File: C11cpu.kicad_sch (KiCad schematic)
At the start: 29 parts, among them IC3 THVD1450DRBR, J1 V24 debug IF, J5 UDPI, U1 AVR64DA48, X1 ASE-24MHz

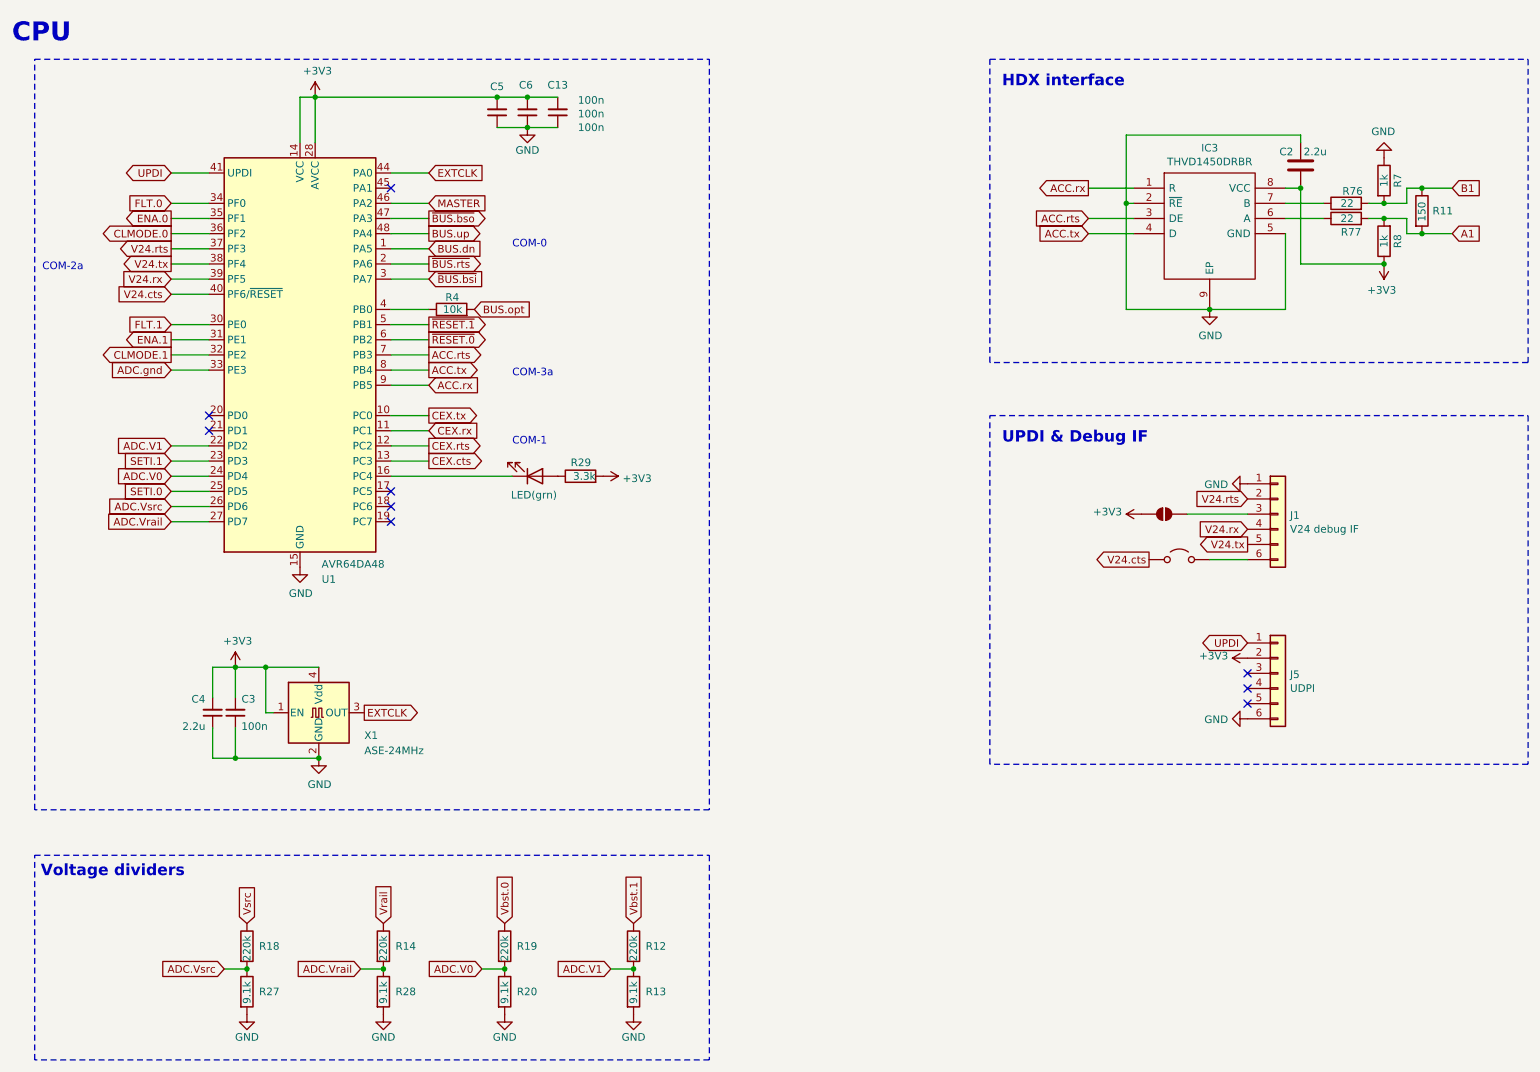
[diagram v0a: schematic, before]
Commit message: mod: changed to buck converter
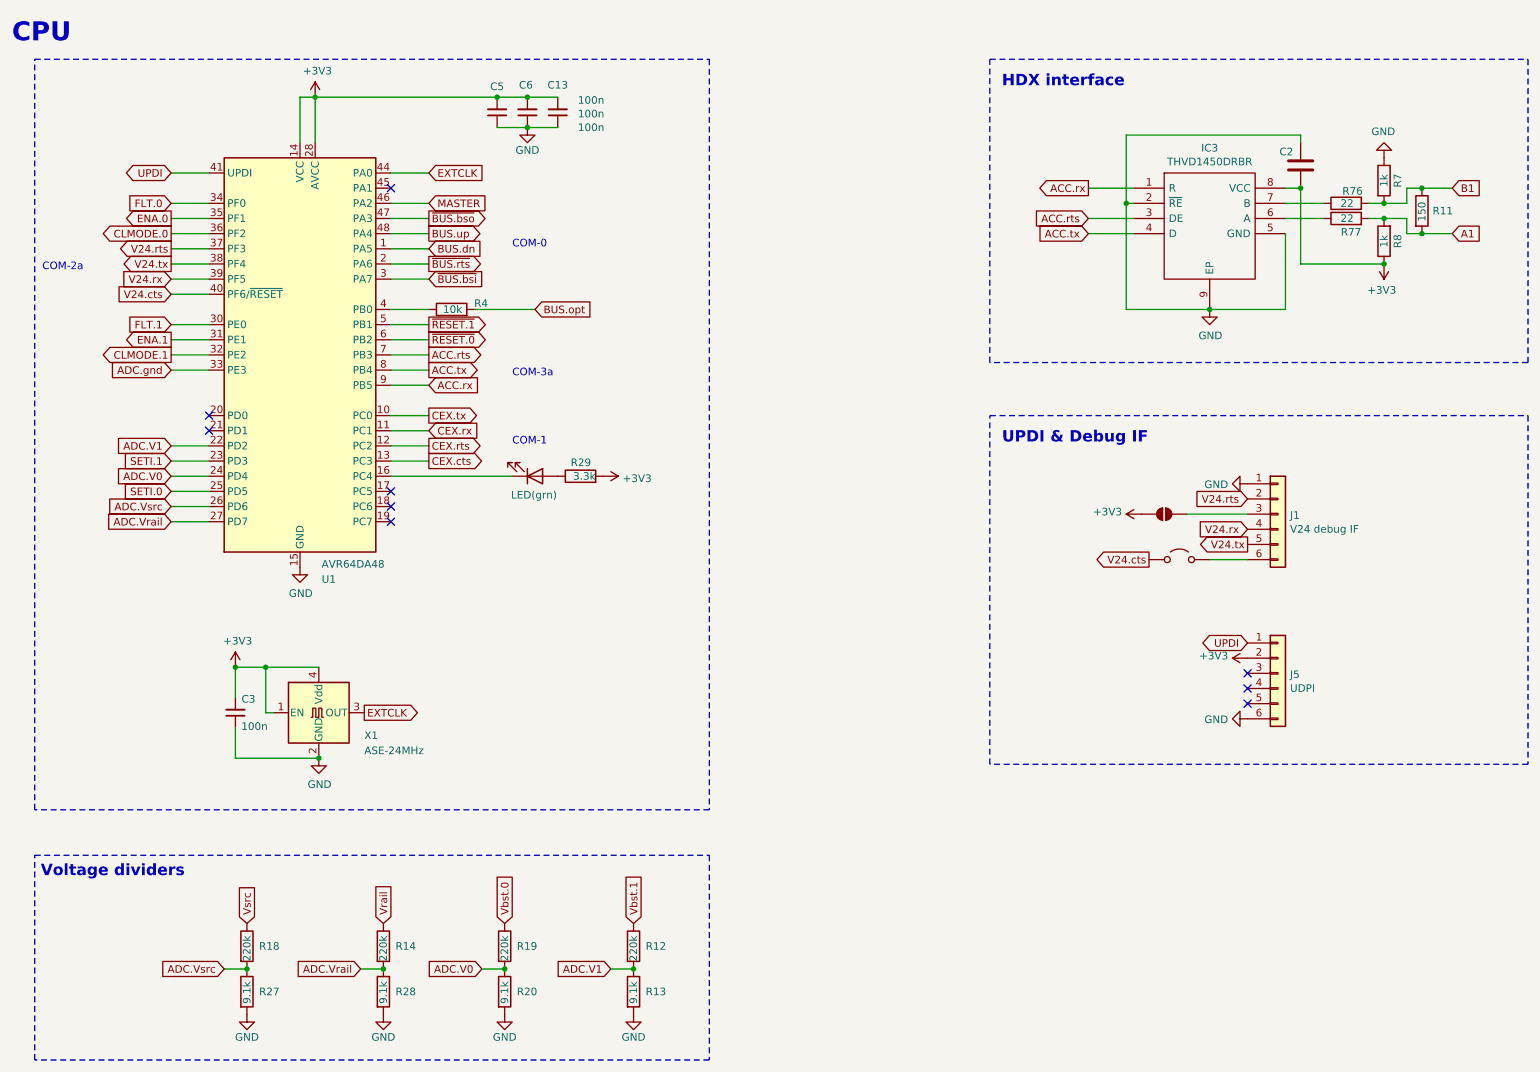
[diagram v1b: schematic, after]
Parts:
- removed C4: 2.2u, Capacitor_SMD:C_0603_1608Metric, symbol Device:C_Small
- C13, C3, C5, C6: LCSC Part # (none) -> C14663
- C2: value 2.2u -> 2.2u/50V; LCSC Part # (none) -> C50254
- D3, J1, J5, JP1, JP2: now left out of the parts list
- IC3: Height 1 -> (none); LCSC Part # (none) -> C1850226; Manufacturer_Name Texas Instruments -> (none); Manufacturer_Part_Number THVD1450DRBR -> (none); Mouser Part Number 595-THVD1450DRBR -> (none); Mouser Price/Stock https://www.mouser.co.uk/ProductDetail/Texas-Instruments/TH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 -> (none)
- R11: LCSC Part # (none) -> C17917
- R12, R14, R18, R19: LCSC Part # (none) -> C22961
- R13, R20, R27, R28: LCSC Part # (none) -> C23260
- R29: LCSC Part # (none) -> C22978
- R4: LCSC Part # (none) -> C25804
- R7, R8: LCSC Part # (none) -> C21190
- R76, R77: LCSC Part # (none) -> C17958
- U1: LCSC Part # (none) -> C3227406
